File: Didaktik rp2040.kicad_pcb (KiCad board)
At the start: 2 copper layers, 209.6 x 76.2 mm, 129 parts, among them J1 Conn_01x04_MountingPin, J2 AVR-ISP-6, J3 Conn_01x03, Q1 2N2222, SW1 SW_Push_45deg, SW10 SW_Push_45deg, SW11 SW_Push_45deg, SW12 SW_Push_45deg, SW13 SW_Push_45deg, SW14 SW_Push_45deg, SW15 SW_Push_45deg, SW16 SW_Push_45deg, SW17 SW_Push_45deg, SW18 SW_Push_45deg, SW19 SW_Push_45deg, SW2 SW_Push_45deg, SW20 SW_Push_45deg, SW21 SW_Push_45deg, SW22 SW_Push_45deg, SW23 SW_Push_45deg, SW24 SW_Push_45deg, SW25 SW_Push_45deg, SW26 SW_Push_45deg, SW27 SW_Push_45deg, SW28 SW_Push_45deg, SW29 SW_Push_45deg, SW3 SW_Push_45deg, SW30 SW_Push_45deg, SW31 SW_Push_45deg, SW31a1 SW_Push_45deg, SW32 SW_Push_45deg, SW32a1 SW_Push_45deg, SW33 SW_Push_45deg, SW33a1 SW_Push_45deg, SW34 SW_Push_45deg, SW34a1 SW_Push_45deg, SW34b1 SW_Push_45deg, SW35 SW_Push_45deg, SW35a1 SW_Push_45deg, SW35b1 SW_Push_45deg, SW35c1 SW_Push_45deg, SW36 SW_Push_45deg, SW36a1 SW_Push_45deg, SW36b1 SW_Push_45deg, SW36c1 SW_Push_45deg, SW37 SW_Push_45deg, SW37a1 SW_Push_45deg, SW37b1 SW_Push_45deg, SW38 SW_Push_45deg, SW38a1 SW_Push_45deg, SW39 SW_Push_45deg, SW39a1 SW_Push_45deg, SW4 SW_Push_45deg, SW40 SW_Push_45deg, SW40a1 SW_Push_45deg, SW41 RotaryEncoder_Switch, SW42 RotaryEncoder_Switch, SW5 SW_Push_45deg, SW6 SW_Push_45deg, SW7 SW_Push_45deg, SW8 SW_Push_45deg, SW9 SW_Push_45deg, U1 ATmega32U4-M, Y1 Crystal_GND24_Small

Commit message: clean up folders, created rp2040 version
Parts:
- removed C2, C5, C7: 0.1uF, Capacitor_SMD:C_0402_1005Metric
- removed C3, C4: 22pF, Capacitor_SMD:C_0402_1005Metric
- removed C8: 10uF, Capacitor_SMD:C_0402_1005Metric
- removed D43: LED, Keebio-Parts:LED_3mm
- removed J2: AVR-ISP-6, random-keyboard-parts:Reset_Pretty-Mask
- removed R3: 10k, Resistor_SMD:R_0402_1005Metric
- removed R8, R9: 220 ohm, Resistor_SMD:R_0402_1005Metric
- removed SW_Reset1: SW_Push, random-keyboard-parts:SKQG-1155865
- removed SW_Reset2: SW_Push, Connector_PinHeader_2.00mm:PinHeader_1x02_P2.00mm_Vertical
- removed Y1: Crystal_GND24_Small, Crystal:Crystal_SMD_3225-4Pin_3.2x2.5mm
- added C10: 22pF, Capacitor_SMD:C_0402_1005Metric, F.Cu at (-39.5, -24.6)
- added C11: 1uF, Capacitor_SMD:C_0402_1005Metric, F.Cu at (-39.5, -22.6)
- added C12: 100nF, Capacitor_SMD:C_0402_1005Metric, F.Cu at (-39.5, -20.6)
- added C13: 1uF, Capacitor_SMD:C_0402_1005Metric, F.Cu at (-39.5, -18.7)
- added C14: 100nF, Capacitor_SMD:C_0402_1005Metric, F.Cu at (-36.7, -28.5)
- added C15: 100nF, Capacitor_SMD:C_0402_1005Metric, F.Cu at (-36.7, -26.5)
- added C16: 10uF, Capacitor_SMD:C_0402_1005Metric, F.Cu at (-36.7, -24.6)
- added C17: 1uF, Capacitor_SMD:C_0402_1005Metric, F.Cu at (-36.7, -22.6)
- added C18: 100nF, Capacitor_SMD:C_0402_1005Metric, F.Cu at (-36.7, -20.6)
- added C19: 100nF, Capacitor_SMD:C_0402_1005Metric, F.Cu at (-36.7, -18.7)
- added C20: 100nF, Capacitor_SMD:C_0402_1005Metric, F.Cu at (-33.8, -28.5)
- added C21: 100nF, Capacitor_SMD:C_0402_1005Metric, F.Cu at (-33.8, -26.5)
- added C22: 100nF, Capacitor_SMD:C_0402_1005Metric, F.Cu at (-33.8, -24.6)
- added C23: 100nF, Capacitor_SMD:C_0402_1005Metric, F.Cu at (-33.8, -22.6)
- added C24: 100nF, Capacitor_SMD:C_0402_1005Metric, F.Cu at (-33.8, -20.6)
- added C9: 22pF, Capacitor_SMD:C_0402_1005Metric, F.Cu at (-39.5, -26.5)
- added J5: SWD, Connector_PinSocket_2.54mm:PinSocket_1x05_P2.54mm_Vertical, F.Cu at (-29.1, -41.3)
- added R10: 27R, Resistor_SMD:R_0603_1608Metric, F.Cu at (-19.9, -30.9)
- added R11: 1k, Resistor_SMD:R_0402_1005Metric, F.Cu at (-19.6, -25.9)
- added R12: 1k, Resistor_SMD:R_0402_1005Metric, F.Cu at (-19.6, -23.9)
- added R7: 27R, Resistor_SMD:R_0603_1608Metric, F.Cu at (-19.9, -33.4)
- added SW43: Reset, Keebio-Parts:SW_SPST_TL3342, F.Cu at (-36.2, -40.1)
- added SW44: Boot, Keebio-Parts:SW_SPST_TL3342, F.Cu at (-36.2, -33.0)
- added U2: RP2040, Sleep-lib:RP2040-QFN-56, F.Cu at (-48.6, 31.5)
- added U3: W25Q128JVS, Package_SO:SOIC-8_5.23x5.23mm_P1.27mm, F.Cu at (-26.2, -25.5)
- added U4: USBLC6-2SC6, Package_TO_SOT_SMD:SOT-23-6, F.Cu at (-24.2, -36.9)
- added U5: 74AHCT1G125, Package_TO_SOT_SMD:TSOT-23-5, F.Cu at (-38.4, -0.44)
- added Y2: 12MHz, Crystal:Crystal_SMD_3225-4Pin_3.2x2.5mm, F.Cu at (-24.2, -41.4)
- C1: value 0.1uF -> 100nF; moved to F.Cu
- C6, D1, D10, D11, D12, D13, D14, D15, D16, D17, D18, D19, D2, D20, D21, D22, D23, D24, D26, D27, D28, D29, D3, D30, D31, D32, D33, D34, D35, D36, D37, D38, D39, D4, D40, D41, D5, D6, D7, D8, D9, F1, J3, LS1, Q1, R6: moved to F.Cu
- D25: value PRTR5V0U2X -> LED; footprint Package_TO_SOT_SMD:SOT-143 -> Keebio-Parts:LED_3mm; moved to F.Cu
- R1: value 22 -> 1k; moved to F.Cu
- R2: value 22 -> 220 ohm; moved to F.Cu
- R4: value 10k -> 220 ohm; moved to F.Cu
- U1: value ATmega32U4-M -> XC6206PxxxMR; footprint Package_DFN_QFN:QFN-44-1EP_7x7mm_P0.5mm_EP5.2x5.2mm -> Package_TO_SOT_SMD:SOT-23; moved to F.Cu
- moved SW10 406.3 mm to (-192.2, 7.54)
- moved SW8 396.8 mm to (-212.4, 128.7)
- moved SW20 394.4 mm to (-172.0, 47.9)
- moved SW9 389.6 mm to (-192.2, -12.7)
- moved SW30 383.6 mm to (-151.8, 88.3)
- moved SW19 376.6 mm to (-172.0, 27.7)
- moved SW7 374.0 mm to (-212.4, 108.5)
- moved SW29 364.7 mm to (-151.8, 68.1)
- moved SW18 360.0 mm to (-172.0, 7.54)
- moved SW6 351.9 mm to (-212.4, 88.3)
- moved SW28 346.9 mm to (-151.8, 47.9)
- moved SW16 345.1 mm to (-192.2, 128.7)
- moved SW17 344.9 mm to (-172.0, -12.7)
- moved SW40a1 343.3 mm to (-111.4, 88.3)
- moved SW5 330.9 mm to (-212.4, 68.1)
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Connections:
- C1 pad 1: +5V -> GND
- C1 pad 2: GND -> +5V
- C6 pad 1: Net-(C6-Pad1) -> +5V
- D25 pad 2: D- -> Net-(D25-A)
- D42 pad 2: Net-(D42-Pad2) -> Net-(D42-A)
- F1 pad 1: VCC -> VBUS
- J1 pad 1: VCC -> VBUS
- J1 pad 2: D- -> D_USB_N
- J1 pad 3: D+ -> D_USB_P
- J3 pad 1: VCC -> +5V
- R1 pad 1: D- -> Net-(C10-Pad2)
- R1 pad 2: Net-(R1-Pad2) -> XTAL_OUT
- R2 pad 1: D+ -> LED capslock
- R2 pad 2: Net-(R2-Pad2) -> Net-(D25-A)
- R4 pad 1: Net-(R4-Pad1) -> LED Power
- R4 pad 2: GND -> Net-(D42-A)
- U1 pad 1: RGB -> GND
- U1 pad 2: +5V -> +3V3
- U1 pad 3: Net-(R1-Pad2) -> +5V
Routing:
- net VCC: track 261.1 -> 0.00 mm, vias 4 -> 0
- net VBUS: track 0.00 -> 261.1 mm, vias 0 -> 4
- net D_USB_P: track 0.00 -> 236.2 mm
- net D+: track 236.2 -> 0.00 mm
- net D-: track 236.0 -> 0.00 mm
- net D_USB_N: track 0.00 -> 235.9 mm
- net (no net): track 0.00 -> 202.1 mm, vias 0 -> 6
- net MOSI: track 58.3 -> 0.00 mm, vias 2 -> 0
- net MISO: track 57.0 -> 0.00 mm, vias 2 -> 0
- net SCK: track 53.4 -> 0.00 mm, vias 2 -> 0
- net COL5: track 192.9 -> 173.9 mm
- net XTAL2: track 10.4 -> 0.00 mm
- net XTAL1: track 8.02 -> 0.00 mm
- net LED capslock: track 225.5 -> 219.9 mm
- net LED Power: track 219.9 -> 225.5 mm
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
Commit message: switch and matrix components placed
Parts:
- C1, C10, C11, C12, C13, C14, C15, C16, C17, C18, C19, C20, C21, C22, C23, C24, C6, C9, D1, D10, D11, D12, D13, D14, D15, D16, D17, D18, D19, D2, D20, D21, D22, D23, D24, D25, D26, D27, D28, D29, D3, D30, D31, D32, D33, D34, D35, D36, D37, D38, D39, D4, D40, D41, D42, D5, D6, D7, D8, D9, F1, J3, J5, LS1, Q1, R1, R10, R11, R12, R2, R4, R6, R7, SW43, SW44, U1, U2, U3, U4, U5, Y2: moved to B.Cu
- moved SW10 406.3 mm to (212.7, 41.3)
- moved SW8 396.8 mm to (174.6, 41.3)
- moved SW20 394.4 mm to (222.2, 60.3)
- moved SW9 389.6 mm to (193.7, 41.3)
- moved SW30 383.6 mm to (231.8, 79.4)
- moved SW19 376.6 mm to (203.2, 60.3)
- moved SWe 374.0 mm to (155.6, 41.3)
- moved SW29 364.7 mm to (212.7, 79.4)
- moved SW18 360.0 mm to (184.2, 60.3)
- moved SW6 352.1 mm to (136.5, 41.3)
- moved SW28 346.9 mm to (193.7, 79.4)
- moved SW16 345.1 mm to (146.1, 60.3)
- moved SW17 344.9 mm to (165.1, 60.3)
- moved SW40a1 343.3 mm to (231.8, 98.4)
- moved SW5 330.9 mm to (117.5, 41.3)
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- renumbered SW7 to SWe
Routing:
- net +5V: track 301.8 -> 1.26 mm, vias 6 -> 0
- net D_USB_N: track 235.9 -> 14.4 mm
- net D_USB_P: track 236.2 -> 16.2 mm
- net RESET: track 223.5 -> 6.09 mm, vias 3 -> 1
- net (no net): track 202.1 -> 0.00 mm, vias 6 -> 0
- net LED capslock: track 219.9 -> 25.4 mm
- net LED Power: track 225.5 -> 31.3 mm
- net GND: track 91.3 -> 17.1 mm, vias 17 -> 10
- net ROTARY_B: track 39.9 -> 10.9 mm, vias 2 -> 0
- net SPEAKER: track 30.0 -> 2.90 mm, vias 2 -> 0
- net ROTARY_A: track 31.8 -> 5.41 mm, vias 2 -> 0
- net ROTARY_C: track 222.1 -> 199.0 mm, vias 2 -> 0
- net ROTARY_D: track 224.8 -> 203.2 mm, vias 2 -> 0
- net COL0: track 105.8 -> 92.6 mm
- net COL1: track 122.9 -> 110.7 mm
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
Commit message: MCU, component placement
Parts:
- moved R12 255.8 mm to (232.3, 48.6)
- moved F1 249.0 mm to (233.9, 44.1), turned to -90 degrees
- moved SW44 243.1 mm to (236.5, 52.2), turned to 90 degrees
- moved C6 237.8 mm to (234.3, 47.4), turned to 0 degrees
- moved C16 234.4 mm to (228.2, 54.6), turned to -90 degrees
- moved C11 233.5 mm to (230.1, 54.2), turned to 0 degrees
- moved C1 226.0 mm to (221.3, 87.7), turned to 90 degrees
- moved U5 222.8 mm to (218.4, 86.2), turned to 0 degrees
- moved Y2 78.8 mm to (50.9, 80.9), turned to 0 degrees
- moved R1 74.7 mm to (48.1, 79.5), turned to 90 degrees
- moved U3 72.8 mm to (55.6, 49.2)
- moved R7 66.4 mm to (42.9, 60.7), turned to -90 degrees
- moved C21 65.2 mm to (55.0, 70.9), turned to 0 degrees
- moved R10 64.6 mm to (41.4, 60.7), turned to -90 degrees
- moved C24 63.4 mm to (54.4, 66.4), turned to 0 degrees
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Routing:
- net COL4: track 174.5 -> 161.5 mm
- net COL2: track 131.1 -> 118.1 mm
- net COL1: track 110.7 -> 97.7 mm
- net COL5: track 165.4 -> 152.4 mm
- net COL3: track 149.5 -> 136.5 mm
- net COL0: track 92.6 -> 82.9 mm
- net COL6: track 200.6 -> 191.0 mm
- net Net-(Q1-B): track 5.80 -> 0.00 mm
- net COL7: track 216.0 -> 210.5 mm
- net COL8: track 235.4 -> 230.0 mm
- net COL9: track 255.0 -> 249.6 mm
- net ROW2: track 380.2 -> 374.9 mm
- net ROW3: track 435.2 -> 430.0 mm
- net ROW0: track 407.6 -> 402.4 mm
- net ROW1: track 381.4 -> 376.3 mm
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- added copper zone on B.Cu, net +1V1
- added copper zone on B.Cu, net +3V3
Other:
- board text added: "place boot correctly"

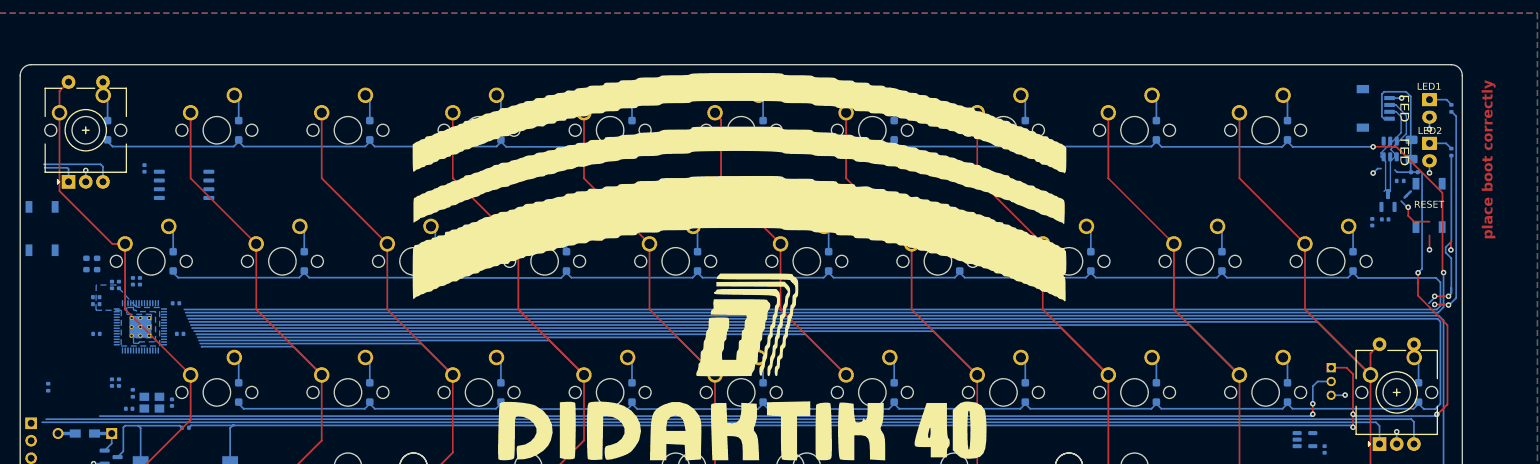
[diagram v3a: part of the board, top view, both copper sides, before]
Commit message: some more cleaner MCU component placement
boot button aligned to plate cut
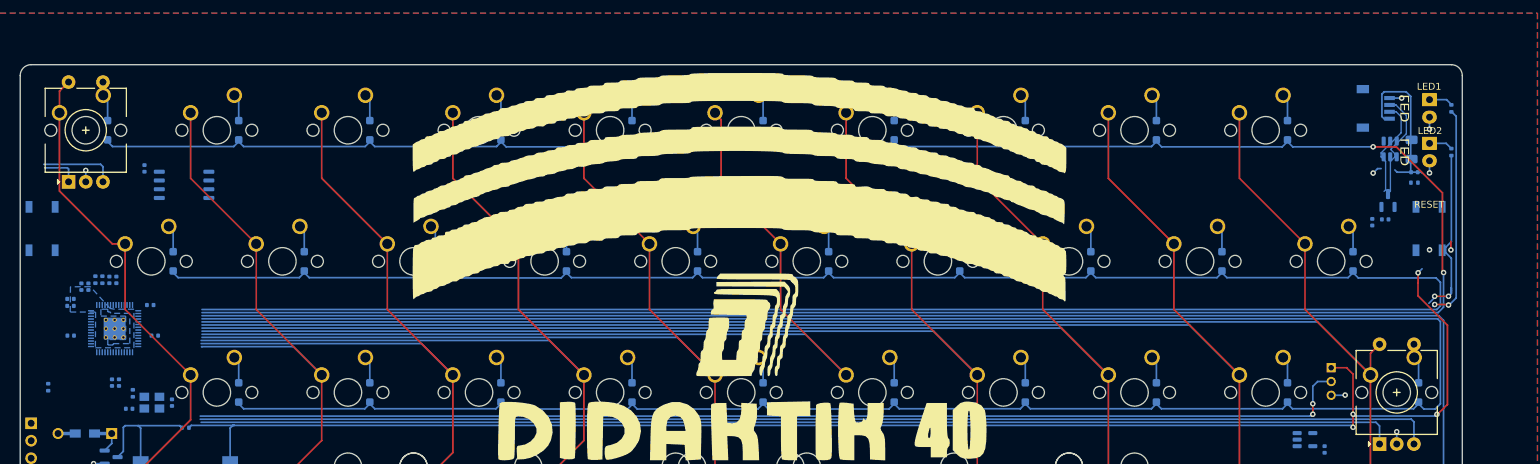
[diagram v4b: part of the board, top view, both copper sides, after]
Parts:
- R10, R7: footprint Resistor_SMD:R_0603_1608Metric -> Resistor_SMD:R_0402_1005Metric
- moved C13 4.45 mm to (41.7, 64.0)
- moved C17 4.45 mm to (40.6, 64.0)
- moved C18 3.75 mm to (39.1, 66.8)
- moved C23 3.75 mm to (39.1, 65.8)
- moved U2 3.75 mm to (45.5, 70.1)
- moved C24 3.75 mm to (50.6, 66.7)
- moved C20 3.75 mm to (39.1, 71.1)
- moved C21 3.69 mm to (51.3, 71.1)
- moved C14 3.43 mm to (45.7, 63.0)
- moved C22 3.43 mm to (44.7, 63.0)
- moved SW44 3.37 mm to (236.5, 55.6)
- moved R10 2.63 mm to (42.7, 63.0)
- moved R7 2.41 mm to (43.7, 63.0)
- moved R12 2.08 mm to (234.3, 48.9)
- renumbered SWe to SW7
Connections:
- net Net-(C10-Pad2) renamed /XTAL_O
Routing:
- net ROTARY_C: track 197.2 -> 174.1 mm
- net ROTARY_D: track 202.1 -> 179.7 mm
- net RGB: track 183.4 -> 168.8 mm
- net VBUS: track 261.1 -> 247.2 mm
- net RESET: track 6.09 -> 0.00 mm, vias 1 -> 0
- net ROW1: track 376.3 -> 373.7 mm
- net ROW0: track 402.4 -> 400.0 mm
- net ROW3: track 430.0 -> 427.8 mm
- net GND: track 17.1 -> 15.0 mm
- net ROW2: track 374.9 -> 372.9 mm
- net COL9: track 249.6 -> 247.8 mm
- net COL8: track 230.0 -> 228.3 mm
- net COL7: track 210.5 -> 209.1 mm
- net /USB_BOOT: track 1.26 -> 0.00 mm
- net COL6: track 191.0 -> 189.8 mm
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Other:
- board text removed: "place boot correctly"
